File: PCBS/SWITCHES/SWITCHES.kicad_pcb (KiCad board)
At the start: 2 copper layers, 29 x 14 mm, 17 parts, among them J1 Conn_01x01_Socket, J2 Conn_01x01_Socket, J3 Conn_01x03_Socket, J6 Conn_01x01_Socket, U1 SN74LVC2G157DCTR

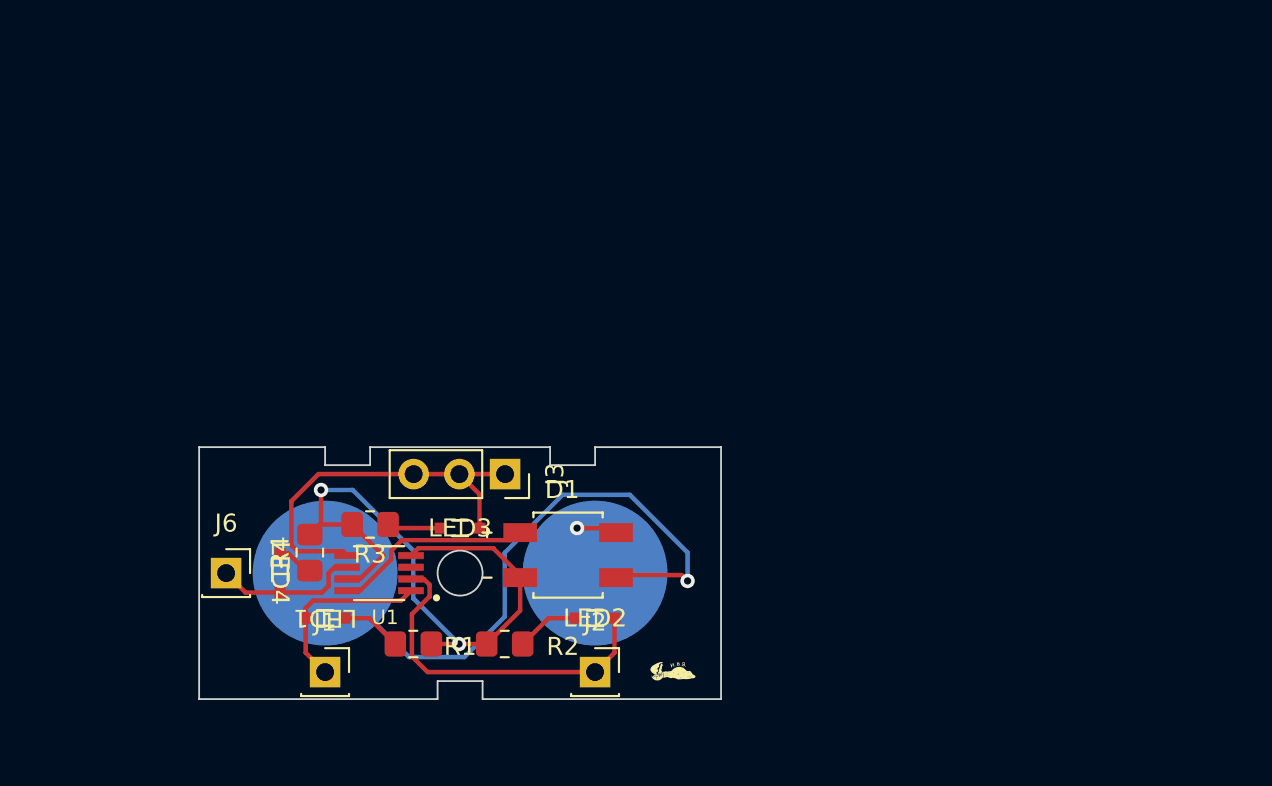
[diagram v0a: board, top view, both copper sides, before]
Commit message: Input PCB layout start
4 Rocker Switches will not fit in 1x2 grid size but rotary switch might
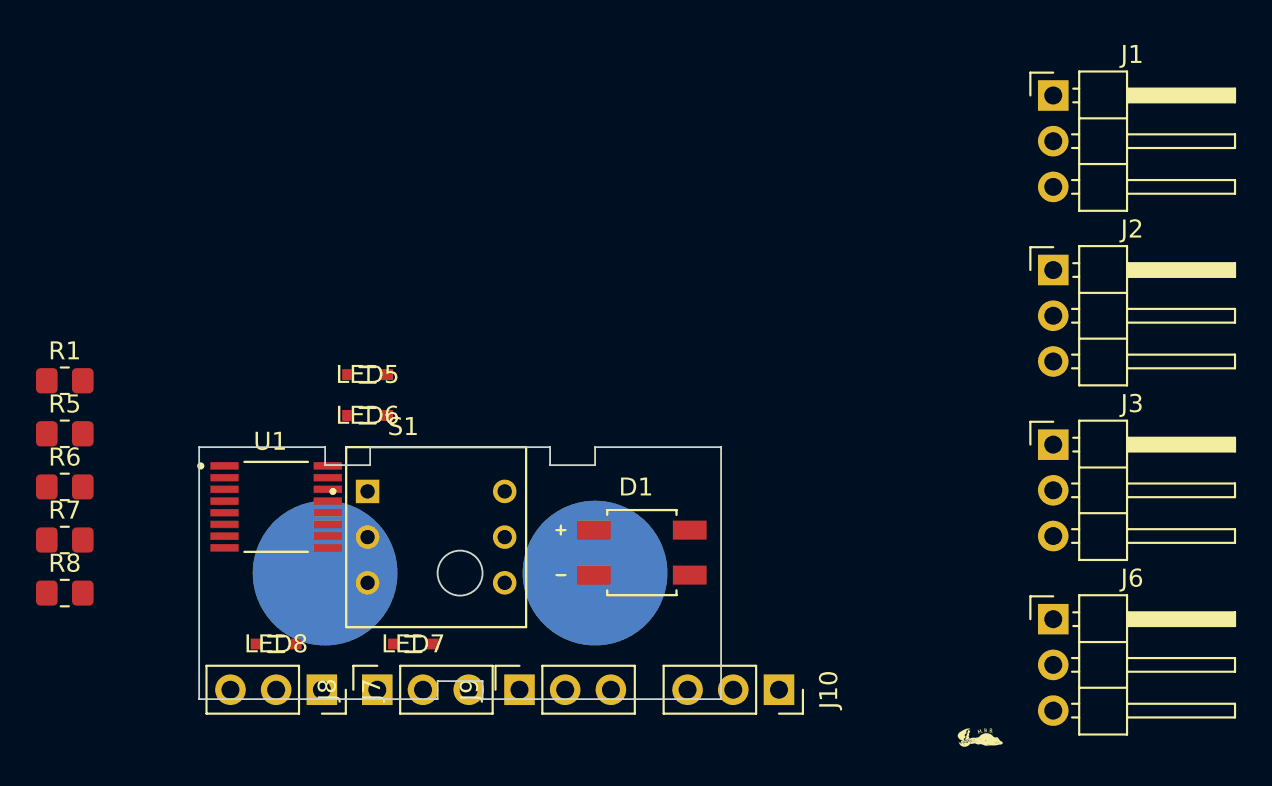
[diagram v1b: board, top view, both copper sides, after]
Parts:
- removed LED1, LED2, LED3, LED4: LTST-S220GKT, DigitalLogicFootprints:LED_LTST-S220GKT_LTO
- removed R2, R3, R4: 4k, Resistor_SMD:R_0805_2012Metric_Pad1.20x1.40mm_HandSolder
- added J10: Conn_01x03_Socket, Connector_PinSocket_2.54mm:PinSocket_1x03_P2.54mm_Vertical, F.Cu at (172.7, 94.0)
- added J7: Conn_01x03_Socket, Connector_PinSocket_2.54mm:PinSocket_1x03_P2.54mm_Vertical, F.Cu at (147.3, 94.0)
- added J8: Conn_01x03_Socket, Connector_PinSocket_2.54mm:PinSocket_1x03_P2.54mm_Vertical, F.Cu at (150.4, 94.0)
- added J9: Conn_01x03_Socket, Connector_PinSocket_2.54mm:PinSocket_1x03_P2.54mm_Vertical, F.Cu at (158.3, 94.0)
- added LED5: LTST-S220GKT, DigitalLogicFootprints:LED_LTST-S220GKT_LTO, F.Cu at (149.9, 76.5)
- added LED6: LTST-S220GKT, DigitalLogicFootprints:LED_LTST-S220GKT_LTO, F.Cu at (149.9, 78.7)
- added LED7: LTST-S220GKT, DigitalLogicFootprints:LED_LTST-S220GKT_LTO, F.Cu at (152.4, 91.4)
- added LED8: LTST-S220GKT, DigitalLogicFootprints:LED_LTST-S220GKT_LTO, F.Cu at (144.8, 91.4)
- added R5: 4k, Resistor_SMD:R_0805_2012Metric_Pad1.20x1.40mm_HandSolder, F.Cu at (133.0, 79.8)
- added R6: 4k, Resistor_SMD:R_0805_2012Metric_Pad1.20x1.40mm_HandSolder, F.Cu at (133.0, 82.7)
- added R7: 4k, Resistor_SMD:R_0805_2012Metric_Pad1.20x1.40mm_HandSolder, F.Cu at (133.0, 85.7)
- added R8: 4k, Resistor_SMD:R_0805_2012Metric_Pad1.20x1.40mm_HandSolder, F.Cu at (133.0, 88.6)
- added S1: RDS-16S-1045-D, DigitalLogicFootprints:SW_RDS-16S-1045-D, F.Cu at (153.7, 85.5)
- J1, J2, J6: value Conn_01x01_Socket -> Conn_01x03_Pin; footprint Connector_PinSocket_2.54mm:PinSocket_1x01_P2.54mm_Vertical -> Connector_PinHeader_2.54mm:PinHeader_1x03_P2.54mm_Horizontal
- J3: value Conn_01x03_Socket -> Conn_01x03_Pin; footprint Connector_PinSocket_2.54mm:PinSocket_1x03_P2.54mm_Vertical -> Connector_PinHeader_2.54mm:PinHeader_1x03_P2.54mm_Horizontal
- R1: value 4k -> 10k
- U1: value SN74LVC2G157DCTR -> CD4043BPWR; footprint DigitalLogicFootprints:SOP65P400X130-8N -> DigitalLogicFootprints:SOP65P640X120-16N
- moved J1 51.6 mm to (188.0, 61.0)
- moved J6 46.0 mm to (188.0, 90.1)
- moved J2 33.9 mm to (188.0, 70.7)
- moved J3 30.5 mm to (188.0, 80.4), turned to 0 degrees
- moved R1 24.3 mm to (133.0, 76.8)
- moved G*** 17.5 mm to (184.1, 96.7)
- moved U1 6.80 mm to (144.8, 83.8), turned to 0 degrees
- moved D1 4.10 mm to (165.1, 86.4)
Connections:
- J1 pad 1: Net-(J1-Pin_1) -> /VCC_RES
- J2 pad 1: Net-(J2-Pin_1) -> /VCC_RES
- J3 pad 1: Net-(J3-Pin_1) -> /VCC_RES
- J3 pad 2: Net-(J3-Pin_1) -> /DEBOUNCE2
- J3 pad 3: Net-(J3-Pin_1) -> GND
- J6 pad 1: Net-(J6-Pin_1) -> /VCC_RES
- R1 pad 1: Net-(LED1-Pad1) -> VCC
- R1 pad 2: GND -> /VCC_RES
- U1 pad 1: Net-(J1-Pin_1) -> /OUTPUT3
- U1 pad 2: Net-(J2-Pin_1) -> /OUTPUT0
- U1 pad 3: unconnected-(U1-~{Y}-Pad3) -> GND
- U1 pad 4: GND -> /DEBOUNCE0
- U1 pad 5: Net-(J3-Pin_1) -> VCC
- U1 pad 6: Net-(J6-Pin_1) -> /DEBOUNCE1
- U1 pad 8: VCC -> GND
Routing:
- net GND: track 37.6 -> 0.00 mm, vias 2 -> 0
- net Net-(J4-PWR): track 34.9 -> 0.00 mm, vias 1 -> 0
- net Net-(J3-Pin_1): track 21.7 -> 0.00 mm
- net Net-(J2-Pin_1): track 19.5 -> 0.00 mm
- net VCC: track 11.3 -> 0.00 mm
- net Net-(J1-Pin_1): track 10.3 -> 0.00 mm
- net Net-(J6-Pin_1): track 8.17 -> 0.00 mm
- net Net-(J5-PWR): track 5.12 -> 0.00 mm, vias 1 -> 0
- net Net-(LED2-Pad1): track 3.54 -> 0.00 mm
- net Net-(LED1-Pad1): track 3.42 -> 0.00 mm
- net Net-(LED3-Pad1): track 3.00 -> 0.00 mm
- net Net-(LED4-Pad1): track 2.04 -> 0.00 mm

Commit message: DRC pass on Inputs
Need to find way to flip headers and add space inbetween headers. That or create way of shorting socket connections without PCB.
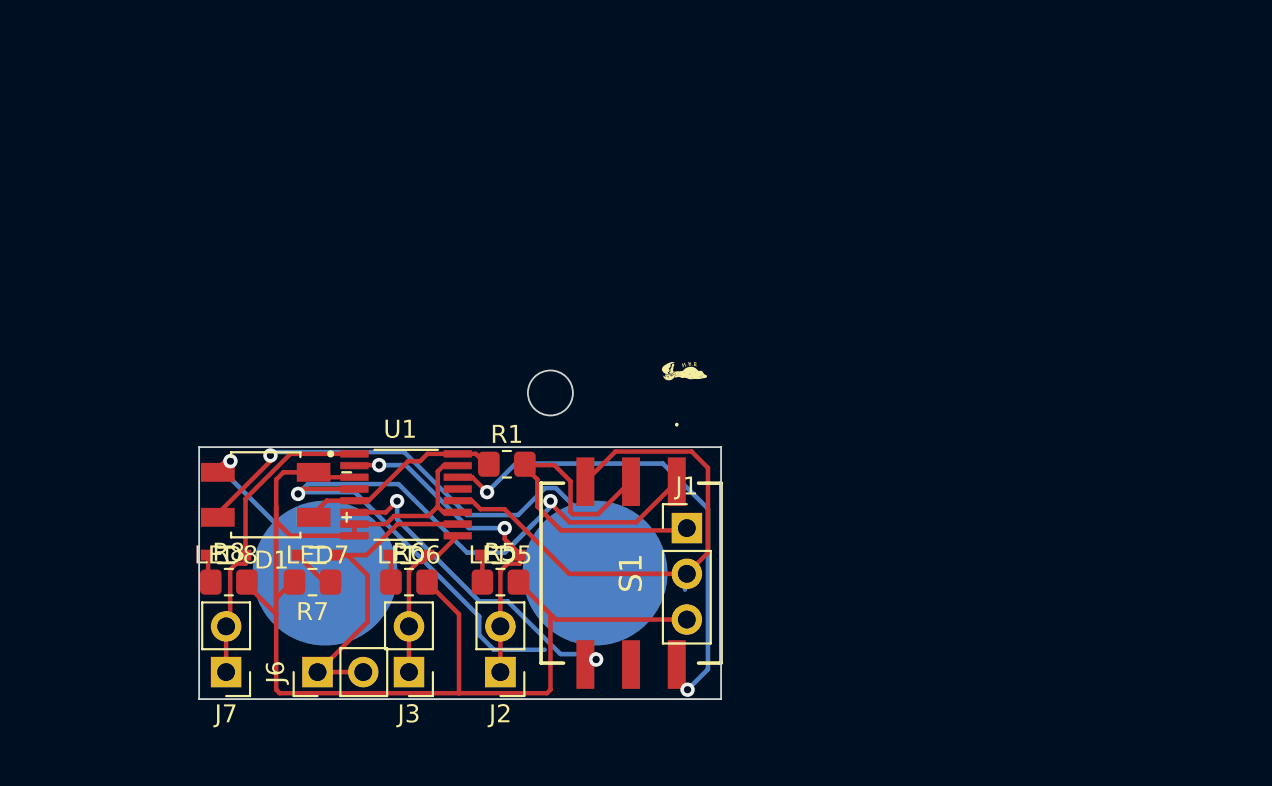
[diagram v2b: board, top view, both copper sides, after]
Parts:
- removed J10, J8, J9: Conn_01x03_Socket, Connector_PinSocket_2.54mm:PinSocket_1x03_P2.54mm_Vertical
- J1: footprint Connector_PinHeader_2.54mm:PinHeader_1x03_P2.54mm_Horizontal -> Connector_PinHeader_2.54mm:PinHeader_1x03_P2.54mm_Vertical
- J2, J3, J6: value Conn_01x03_Pin -> Conn_01x02_Socket; footprint Connector_PinHeader_2.54mm:PinHeader_1x03_P2.54mm_Horizontal -> Connector_PinHeader_2.54mm:PinHeader_1x02_P2.54mm_Vertical
- J7: value Conn_01x03_Socket -> Conn_01x02_Socket; footprint Connector_PinSocket_2.54mm:PinSocket_1x03_P2.54mm_Vertical -> Connector_PinHeader_2.54mm:PinHeader_1x02_P2.54mm_Vertical
- S1: value RDS-16S-1045-D -> RDS-16S-1055-SMT; footprint DigitalLogicFootprints:SW_RDS-16S-1045-D -> DigitalLogicFootprints:RDS16S1055SMT
- moved J6 41.0 mm to (147.1, 93.0), turned to 90 degrees
- moved J2 38.0 mm to (157.2, 93.0), turned to 180 degrees
- moved J3 38.0 mm to (152.2, 93.0), turned to 180 degrees
- moved J1 31.5 mm to (167.6, 85.0)
- moved G*** 26.2 mm to (167.6, 76.3)
- moved R5 25.6 mm to (157.2, 88.0)
- moved R1 25.0 mm to (157.6, 81.5)
- moved D1 21.1 mm to (144.2, 83.2), turned to 180 degrees
- moved R6 19.8 mm to (152.2, 88.0)
- moved R7 14.0 mm to (146.8, 88.0), turned to 180 degrees
- moved LED5 12.5 mm to (157.2, 86.5)
- moved S1 11.0 mm to (164.5, 87.5), turned to -90 degrees
- moved R8 9.14 mm to (142.2, 88.0)
- moved LED6 8.09 mm to (152.2, 86.5)
- moved LED7 7.26 mm to (147.1, 86.5)
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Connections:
- J1 pad 2: /DEBOUNCE0 -> /DEBOUNCE2
- J2 pad 1: /VCC_RES -> /OUTPUT0
- J2 pad 2: /DEBOUNCE1 -> /OUTPUT0
- J3 pad 1: /VCC_RES -> /OUTPUT1
- J3 pad 2: /DEBOUNCE2 -> /OUTPUT1
- J6 pad 1: /VCC_RES -> /OUTPUT2
- J6 pad 2: /DEBOUNCE3 -> /OUTPUT2
- J7 pad 1: /OUTPUT0 -> /OUTPUT3
- J7 pad 2: /OUTPUT0 -> /OUTPUT3
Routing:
- net GND: track 0.00 -> 73.4 mm
- net /DEBOUNCE0: track 0.00 -> 49.1 mm, vias 0 -> 2
- net Net-(J5-PWR): track 0.00 -> 31.0 mm, vias 0 -> 1
- net /DEBOUNCE2: track 0.00 -> 30.2 mm
- net /DEBOUNCE3: track 0.00 -> 26.5 mm, vias 0 -> 2
- net /VCC_RES: track 0.00 -> 21.2 mm
- net /OUTPUT0: track 0.00 -> 19.0 mm, vias 0 -> 2
- net /OUTPUT2: track 0.00 -> 18.7 mm
- net /DEBOUNCE1: track 0.00 -> 18.1 mm, vias 0 -> 2
- net /OUTPUT3: track 0.00 -> 17.5 mm
- net VCC: track 0.00 -> 11.6 mm
- net Net-(J4-PWR): track 0.00 -> 9.56 mm, vias 0 -> 1
- net /OUTPUT1: track 0.00 -> 9.16 mm
- net Net-(LED7-Pad1): track 0.00 -> 2.56 mm
- net Net-(LED8-Pad1): track 0.00 -> 1.53 mm
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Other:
- board size 29 x 14 mm -> 29 x 18.3 mm

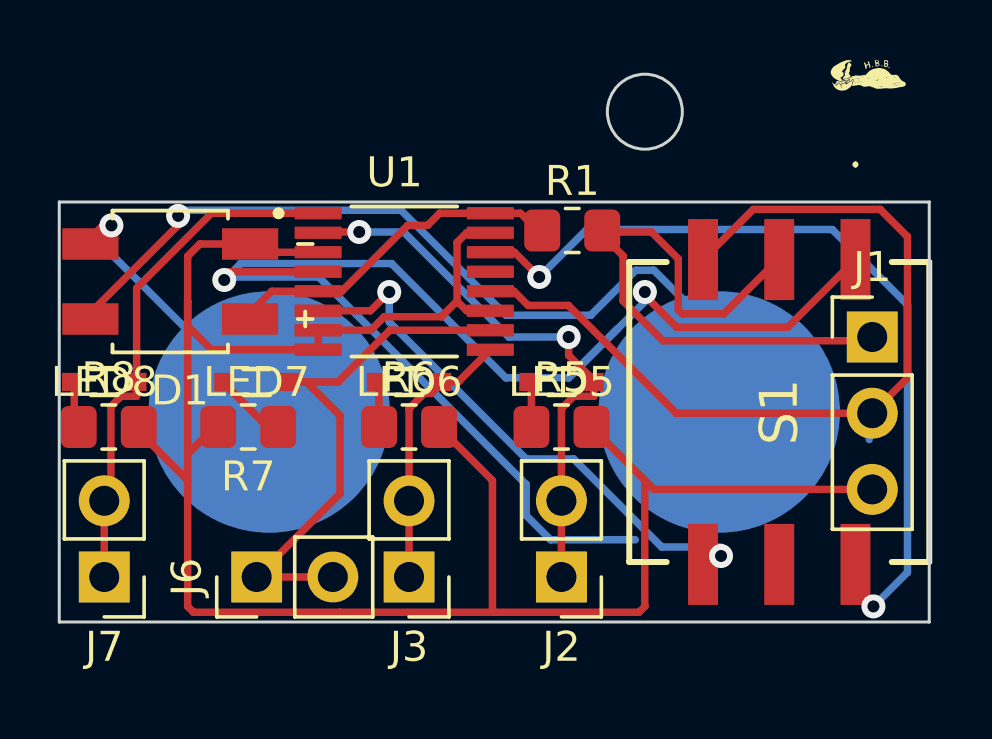
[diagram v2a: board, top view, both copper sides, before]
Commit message: Added Screw Hole
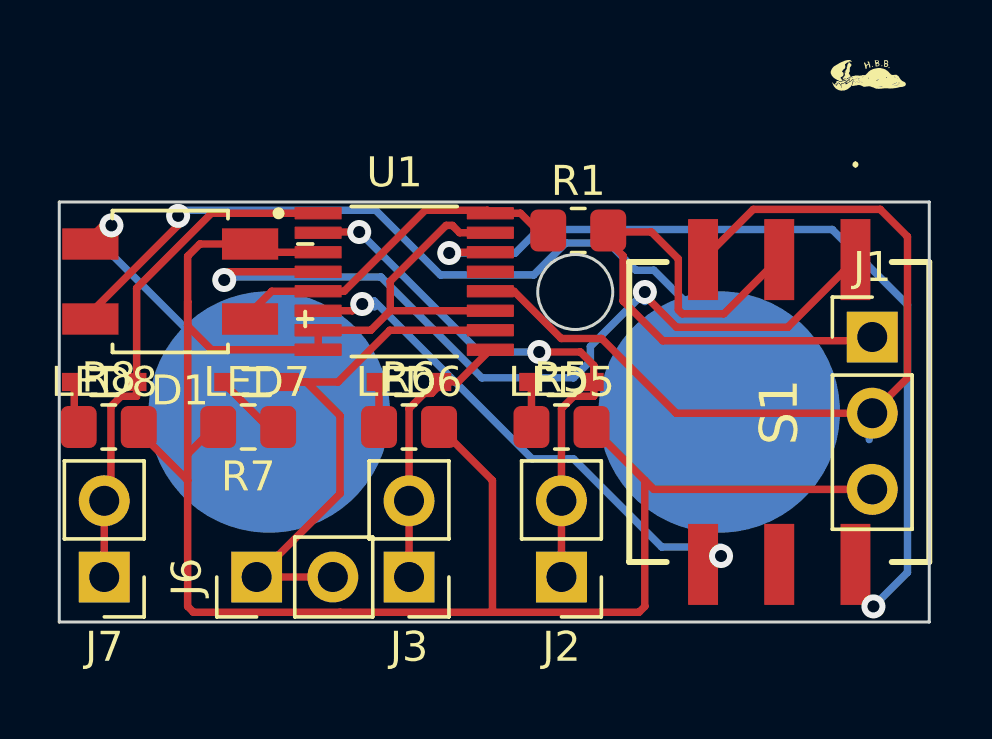
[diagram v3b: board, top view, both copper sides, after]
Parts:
- moved R1 0.20 mm to (157.8, 81.5)
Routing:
- net /DEBOUNCE0: track 49.1 -> 28.9 mm
- net /DEBOUNCE3: track 26.5 -> 28.5 mm
- net GND: track 73.4 -> 75.2 mm
- net /DEBOUNCE1: track 18.1 -> 17.0 mm
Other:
- board size 29 x 18.3 mm -> 29 x 14 mm

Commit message: move Logo
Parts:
- G***: moved to B.Cu
- moved G*** 17.8 mm to (165.1, 94.0), turned to 180 degrees

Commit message: Completed. SilkScreen changes necessary
Uses one SMD right pin header socket for the rotary switch
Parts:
- added J8: Conn_01x03_Socket, Connector_PinSocket_2.54mm:PinSocket_1x03_P2.54mm_Vertical, F.Cu at (152.2, 93.0)
- J2: footprint Connector_PinHeader_2.54mm:PinHeader_1x02_P2.54mm_Vertical -> Connector_PinSocket_2.54mm:PinSocket_1x02_P2.54mm_Vertical
- J6: footprint Connector_PinHeader_2.54mm:PinHeader_1x02_P2.54mm_Vertical -> Connector_PinSocket_2.54mm:PinSocket_1x02_P2.54mm_Vertical_SMD_Pin1Right
- moved J6 1.27 mm to (147.1, 91.7), turned to 0 degrees
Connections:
- J1 pad 2: /DEBOUNCE2 -> /DEBOUNCE1
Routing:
- net /DEBOUNCE1: track 17.0 -> 26.8 mm
- net /OUTPUT1: track 9.16 -> 14.2 mm
- net GND: track 75.2 -> 78.2 mm
- net /OUTPUT2: track 18.7 -> 18.1 mm

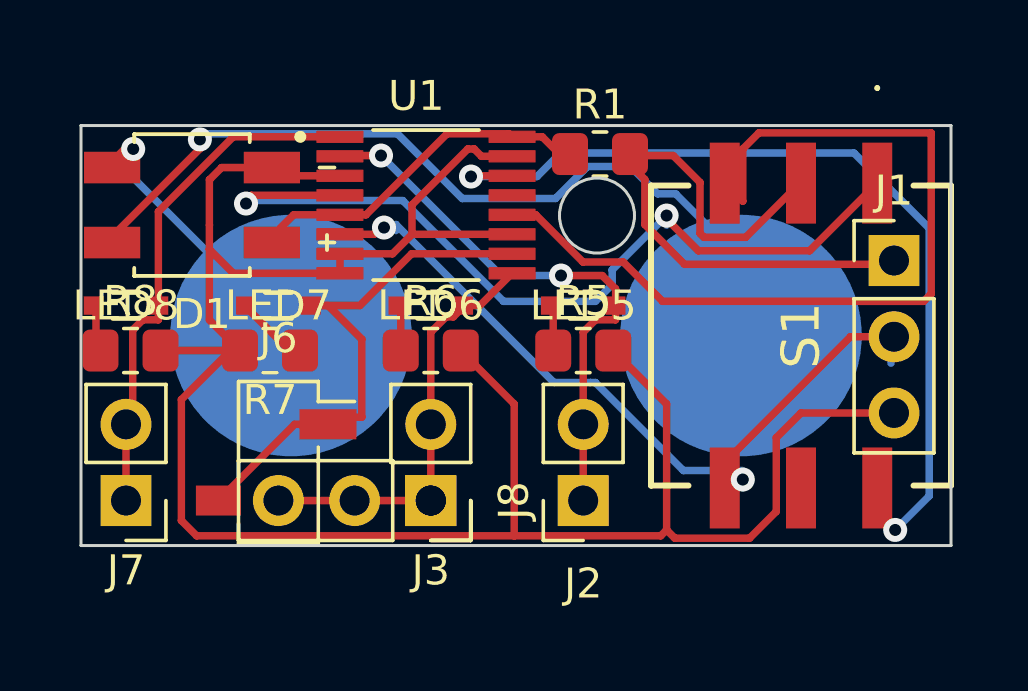
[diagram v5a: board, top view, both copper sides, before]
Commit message: Finished input PCB and fixed mux and not
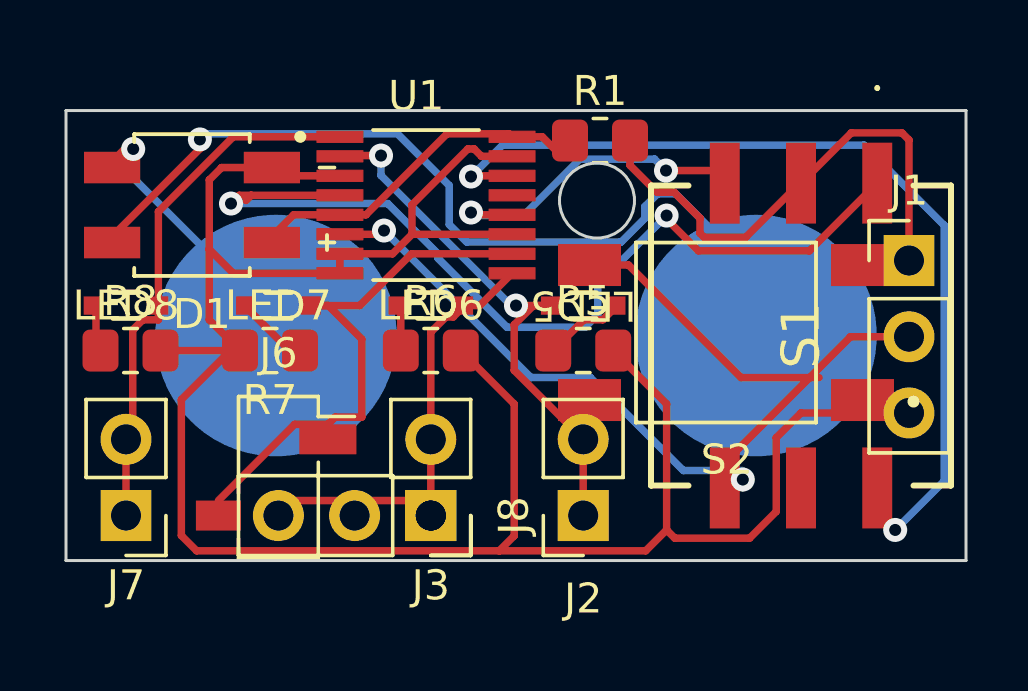
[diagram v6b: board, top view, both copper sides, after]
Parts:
- added S2: 1571527-2, DigitalLogicFootprints:SW_1571527-2, F.Cu at (162.0, 87.4)
- moved J1 0.50 mm to (168.1, 85.0)
- moved J2 0.50 mm to (157.2, 93.5)
- moved J3 0.50 mm to (152.2, 93.5)
- moved J4 0.50 mm to (147.0, 87.5)
- moved J5 0.50 mm to (163.0, 87.5)
- moved J6 0.50 mm to (147.1, 92.2)
- moved J7 0.50 mm to (142.0, 93.5)
- moved J8 0.50 mm to (152.2, 93.5)
- moved R1 0.45 mm to (157.8, 81.0)
- turned LED5 to 180 degrees
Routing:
- net /DEBOUNCE2: track 29.7 -> 11.5 mm, vias 0 -> 2
- net /DEBOUNCE1: track 26.8 -> 35.2 mm
- net /VCC_RES: track 21.2 -> 18.0 mm
- net /DEBOUNCE3: track 28.5 -> 31.2 mm
- net /DEBOUNCE0: track 28.9 -> 31.1 mm
- net Net-(J5-PWR): track 30.6 -> 32.0 mm
- net GND: track 78.2 -> 79.6 mm
- net Net-(LED5-Pad1): track 1.53 -> 2.78 mm
- net /OUTPUT0: track 19.0 -> 18.4 mm
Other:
- board size 29 x 14 mm -> 30 x 15 mm
